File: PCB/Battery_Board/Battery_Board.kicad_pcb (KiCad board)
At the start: 2 copper layers, 90 x 83.5 mm, 8 parts, among them J1 SE2-30, U1 LTC4451AV-TRPBF

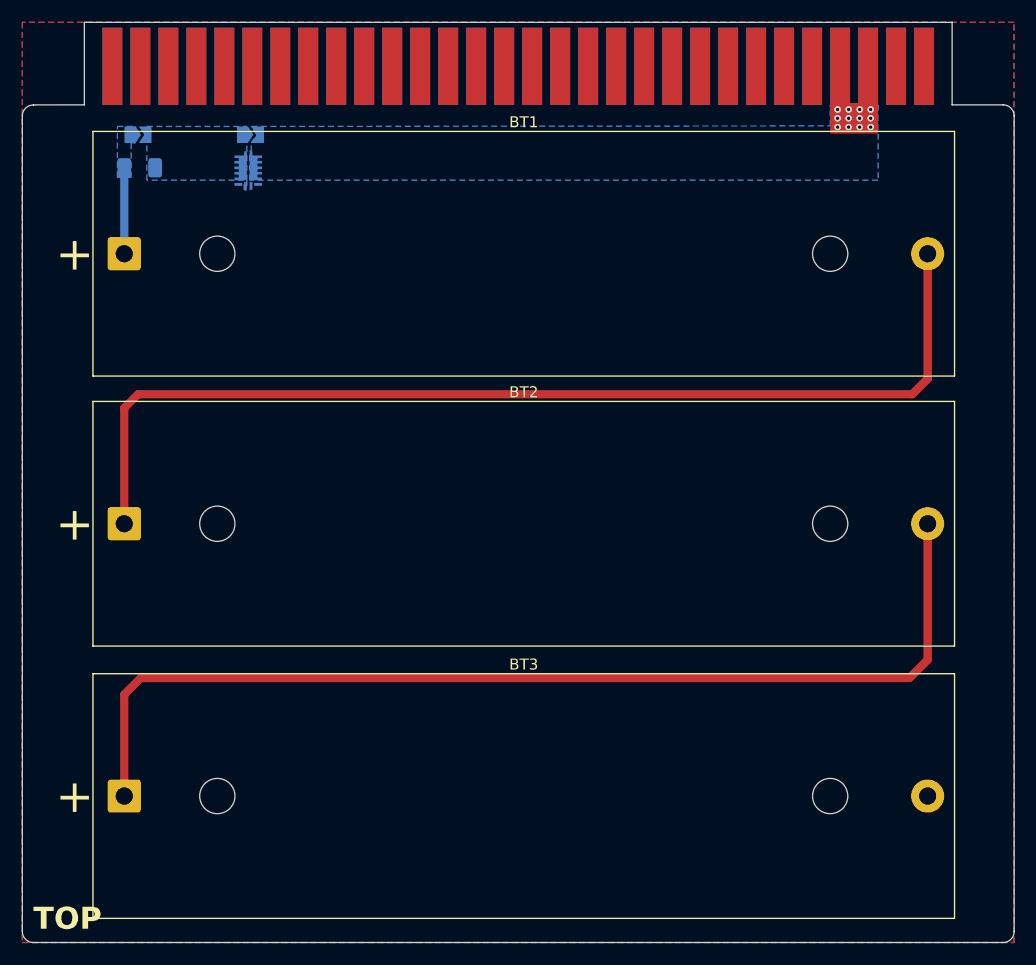
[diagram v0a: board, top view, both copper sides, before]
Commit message: Updated battery board to include ATtiny MCU for current and voltage monitoring. Updated SE2-30 footprint's silkscreen.
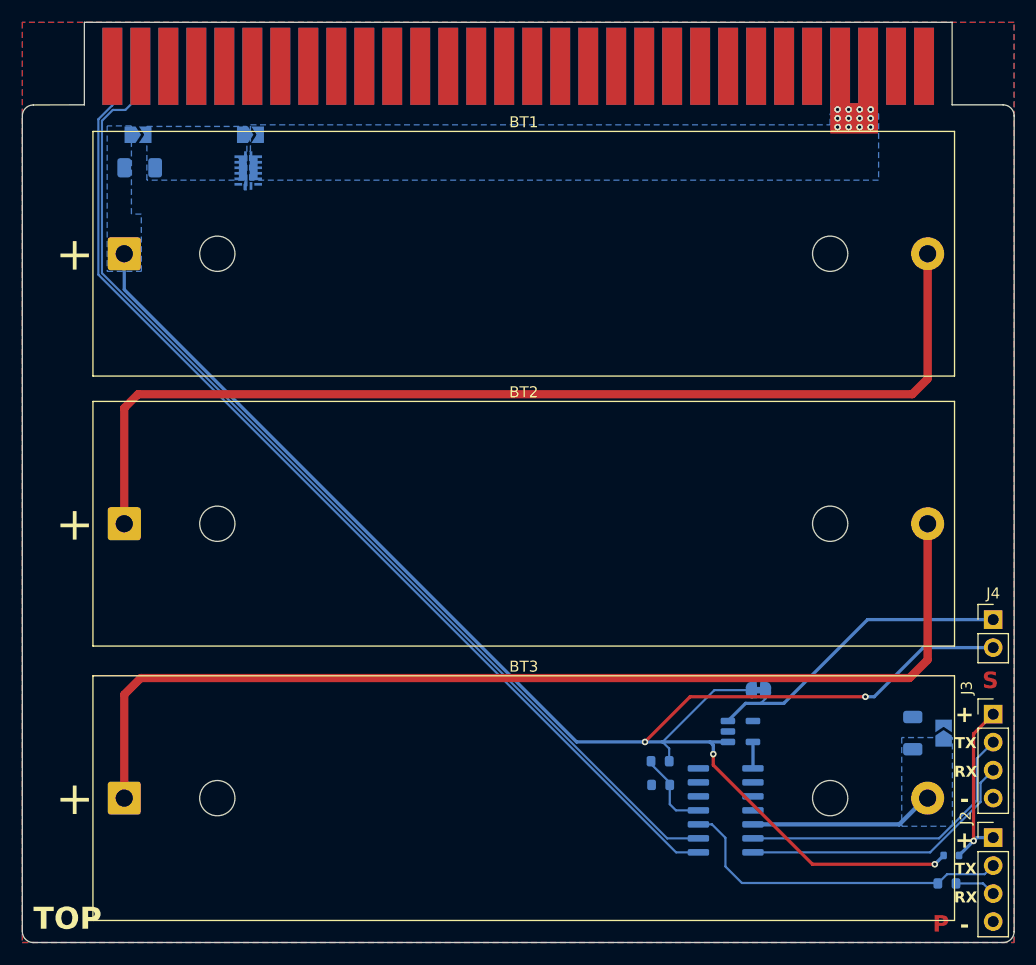
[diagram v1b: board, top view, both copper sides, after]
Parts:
- added D1: BAT54WX-TP, Diode_SMD:D_SOD-523, B.Cu at (256.8, 117.6)
- added J2: UDPI, Connector_PinHeader_2.54mm:PinHeader_1x04_P2.54mm_Vertical, F.Cu at (260.6, 116.0)
- added J3: UART0, Connector_PinHeader_2.54mm:PinHeader_1x04_P2.54mm_Vertical, F.Cu at (260.6, 104.8)
- added J4: MCU En/Disable, Connector_PinHeader_2.54mm:PinHeader_1x02_P2.54mm_Vertical, F.Cu at (260.6, 96.2)
- added JP3: Shunt Resistor Bypass, Jumper:SolderJumper-2_P1.3mm_Open_TrianglePad1.0x1.5mm, B.Cu at (256.1, 106.5)
- added JP4: MCU Disable, Jumper:SolderJumper-2_P1.3mm_Bridged_RoundedPad1.0x1.5mm, B.Cu at (239.3, 102.6)
- added R1: 1k, Resistor_SMD:R_0603_1608Metric, B.Cu at (256.4, 120.1)
- added R2: 0.02, Resistor_SMD:R_1206_3216Metric, B.Cu at (253.3, 106.5)
- added R3: 3.3k, Resistor_SMD:R_0603_1608Metric, B.Cu at (230.4, 109.0)
- added R4: 680, Resistor_SMD:R_0603_1608Metric, B.Cu at (230.4, 111.2)
- added U3: ATtiny1624-SS, Package_SO:SOIC-14_3.9x8.7mm_P1.27mm, B.Cu at (236.3, 113.5)
- added U4: MIC5205-3.3YM5, Package_TO_SOT_SMD:SOT-23-5, B.Cu at (237.7, 106.3)
- JP1: renamed from Fuse BP; value SolderJumper_2_Open -> Fuse Bypass
- JP2: renamed from Diode BP; value SolderJumper_2_Open -> Ideal Diode Bypass
- moved BT3 0.19 mm to (181.8, 112.4)
- turned F1 to 180 degrees
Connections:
- BT3 pad 2: GND -> /SHUNT+
- F1 pad 1: +BATT -> Net-(JP1-B)
- F1 pad 2: Net-(JP1-B) -> +BATT
- J1 pad 31: unconnected-(J1-GPIO_2-Pad31) -> /MCU_SDA
- J1 pad 32: unconnected-(J1-GPIO_3-Pad32) -> /MCU_SCL
- U1 pad 15: unconnected-(U1-STATUS-Pad15) -> GND
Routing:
- net +BATT: track 7.80 -> 149.4 mm, vias 0 -> 4
- net /MCU_SCL: track 0.00 -> 96.2 mm
- net /MCU_SDA: track 0.00 -> 95.6 mm
- net /IN_PGM_RX: track 0.00 -> 31.2 mm
- net /MCU_PWR_EN: track 0.00 -> 29.3 mm
- net /MCU_RX: track 0.00 -> 27.7 mm
- net /MCU_TX: track 0.00 -> 25.9 mm
- net /SHUNT+: track 0.00 -> 16.9 mm
- net /USB_PWR: track 0.00 -> 16.0 mm, vias 0 -> 1
- net /DIVIDER+: track 0.00 -> 7.44 mm
- net /IN_PGM_TX: track 0.00 -> 3.76 mm
- net Net-(JP1-B): track 0.00 -> 2.92 mm
- net +3.3V: track 0.00 -> 2.40 mm
- added copper zone on B.Cu, net /SHUNT+
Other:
- board text added: "+"
- board text added: "-"
- board text added: "Current/Voltage Monitor"
- board text added: "P"
- board text added: "RX"
- board text added: "S"
- board text added: "TX"

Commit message: Small improvements
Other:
- board text added: "← Shunt"
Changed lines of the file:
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@@
 	)
 	(paper "A4")
+	(title_block
+		(title "Battery Board")
+		(date "2026-10-31")
+		(rev "2.0a")
+		(company "UNL Aerospace Rocketry")
+	)
 	(layers
 		(0 "F.Cu" signal)
@@
 		(tags "resistor")
 		(property "Reference" "R4"
-			(at 0.025 -1.6 0)
+			(at 1.325 -1.6 0)
 			(layer "B.SilkS")
 			(effects
@@
 		(tags "resistor")
 		(property "Reference" "R3"
-			(at 0.025 1.35 0)
+			(at 1.275 1.35 0)
 			(layer "B.SilkS")
 			(effects
@@
 		)
 	)
+	(gr_text "← Shunt"
+		(at 251.8 106.5 0)
+		(layer "B.SilkS")
+		(effects
+			(font
+				(size 1 1)
+				(thickness 0.15)
+			)
+			(justify left mirror)
+		)
+	)
 	(gr_text "Current/Voltage Monitor"
 		(at 262.3 102.8 0)
@@
 		(start 231.2 109.05)
 		(end 231.2 107.9)
-		(width 0.2)
+		(width 0.3)
 		(layer "B.Cu")
 		(net "+BATT")
@@
 		(start 238.65 102.6)
 		(end 235.3 102.6)
-		(width 0.2)
+		(width 0.3)
 		(layer "B.Cu")
 		(net "+BATT")
@@
 		(start 230.6 107.3)
 		(end 235.3 102.6)
-		(width 0.2)
+		(width 0.3)
 		(layer "B.Cu")
 		(net "+BATT")
@@
 		(start 231.2 107.9)
 		(end 230.6 107.3)
-		(width 0.2)
+		(width 0.3)
 		(layer "B.Cu")
 		(net "+BATT")
@@
 		(start 239.95 103.355)
 		(end 239.505 103.8)
-		(width 0.2)
+		(width 0.3)
 		(layer "B.Cu")
 		(net "/MCU_PWR_EN")
@@
 		(start 239.95 102.6)
 		(end 239.95 103.355)
-		(width 0.2)
+		(width 0.3)
 		(layer "B.Cu")
 		(net "/MCU_PWR_EN")
@@
 	)
 	(segment
+		(start 252.081029 114.78)
+		(end 254.651029 112.21)
+		(width 0.4)
+		(layer "B.Cu")
+		(net "/SHUNT+")
+	)
+	(segment
+		(start 238.8 114.78)
+		(end 252.081029 114.78)
+		(width 0.4)
+		(layer "B.Cu")
+		(net "/SHUNT+")
+	)
+	(segment
 		(start 192.75 56.85)
 		(end 192.75 54.850001)
@@
 	)
 	(segment
-		(start 252.081029 114.78)
-		(end 254.651029 112.21)
-		(width 0.4)
-		(layer "B.Cu")
-		(net "/SHUNT+")
-	)
-	(segment
-		(start 238.8 114.78)
-		(end 252.081029 114.78)
-		(width 0.4)
-		(layer "B.Cu")
-		(net "/SHUNT+")
-	)
-	(segment
 		(start 231.25 112.95)
 		(end 231.25 111.2)
-		(width 0.2)
+		(width 0.3)
 		(layer "B.Cu")
 		(net "/DIVIDER+")
@@
 		(start 231.25 111)
 		(end 229.55 109.3)
-		(width 0.2)
+		(width 0.3)
 		(layer "B.Cu")
 		(net "/DIVIDER+")
@@
 		(start 231.81 113.51)
 		(end 231.25 112.95)
-		(width 0.2)
+		(width 0.3)
 		(layer "B.Cu")
 		(net "/DIVIDER+")
@@
 		(start 233.85 113.51)
 		(end 231.81 113.51)
-		(width 0.2)
+		(width 0.3)
 		(layer "B.Cu")
 		(net "/DIVIDER+")
@@
 		(fill yes
 			(thermal_gap 0.5)
-			(thermal_bridge_width 0.5)
+			(thermal_bridge_width 1)
 			(island_removal_mode 0)
 		)
